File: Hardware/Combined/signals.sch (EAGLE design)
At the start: 108 parts, among them IC2_AUD 74LS32N, IC36 4040N, IC37 74AS30N, IC39 7400N, IC40 4040N, IC41 7400N, IC43 7400N, IC44 7486N, IC45 7400N, IC46 74S257N, IC47 74S257N, IC48 74HC564N, IC4_AUD 7400N, IC53 7404N, IC6_AUD 74S74N, IC7_AUD LM358N, J2 TX24-40R-12ST-H1E, U1 W65C02SP

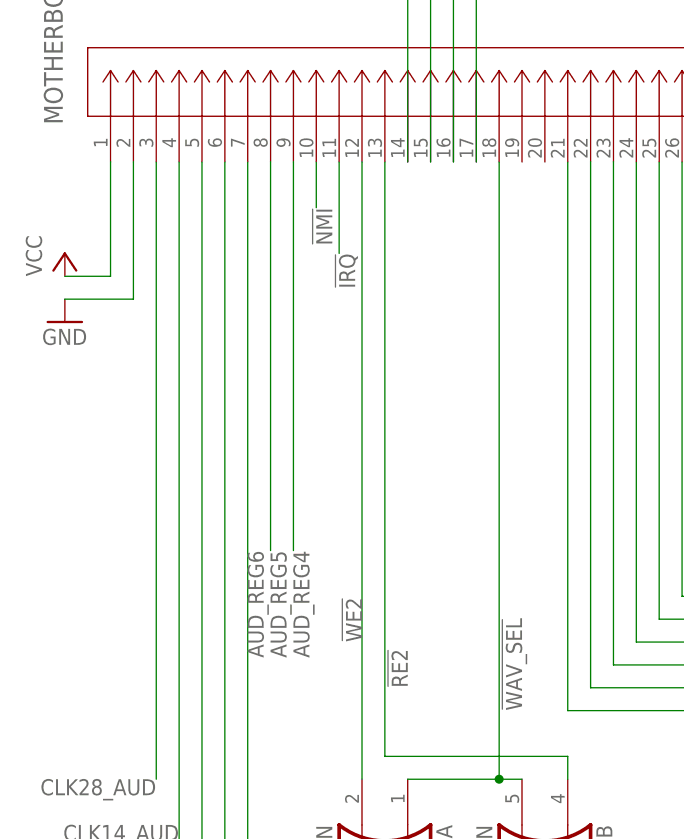
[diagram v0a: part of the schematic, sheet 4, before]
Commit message: Updates to combined board inc. new blitter features
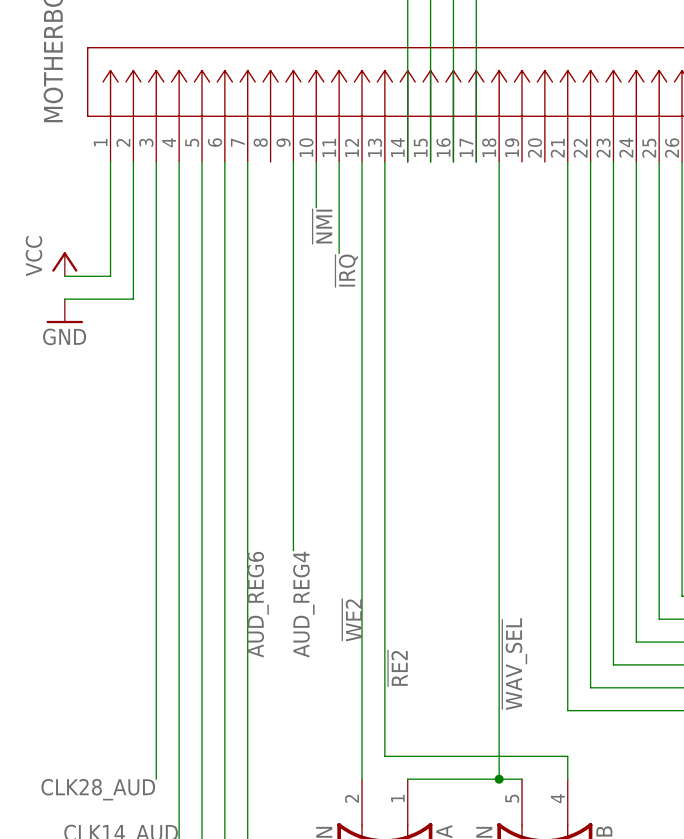
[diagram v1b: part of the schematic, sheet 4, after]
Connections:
- removed net AUD_REG5: MOTHERBOARD.8
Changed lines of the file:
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@@
-</segment>
-</net>
-<net name="AUD_REG5" class="0">
-<segment>
-<pinref part="MOTHERBOARD" gate="A" pin="8"/>
-<wire x1="-99.06" y1="124.46" x2="-99.06" y2="81.28" width="0.1524" layer="91"/>
-<label x="-99.06" y="81.28" size="1.778" layer="95" rot="R270"/>
 </segment>
 </net>
